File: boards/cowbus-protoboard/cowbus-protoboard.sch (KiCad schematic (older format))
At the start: 9 parts

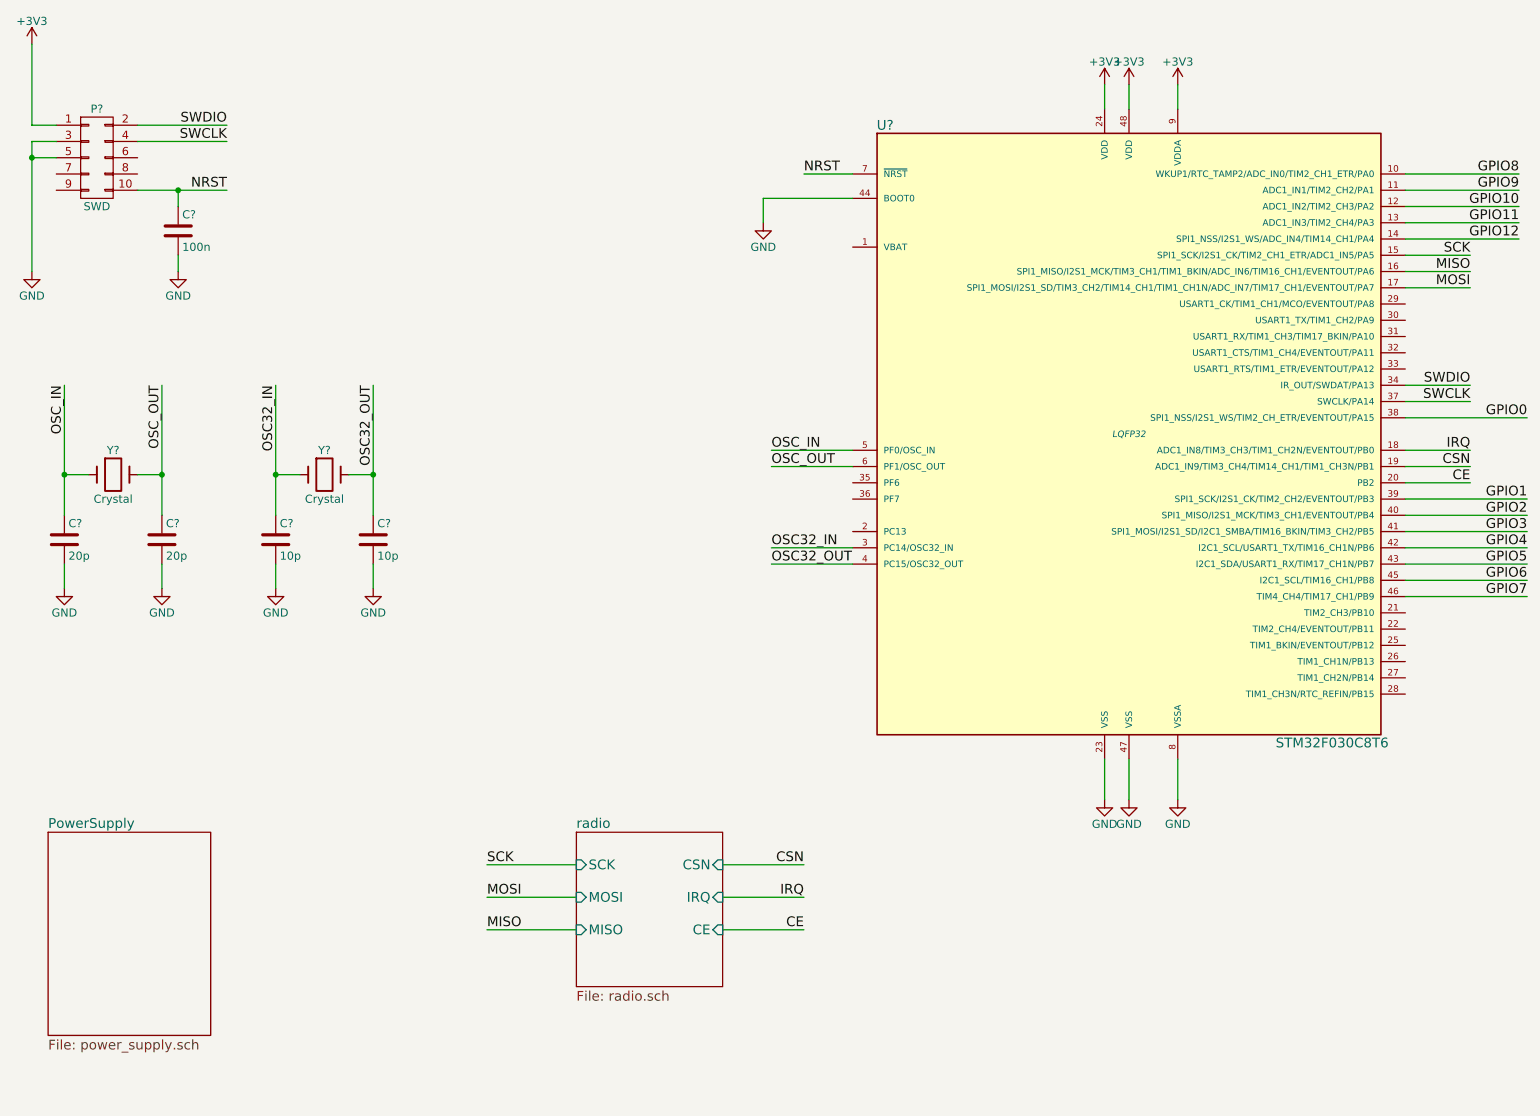
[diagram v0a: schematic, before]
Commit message: mad emcu second hierarchy, added top level, added empty periph
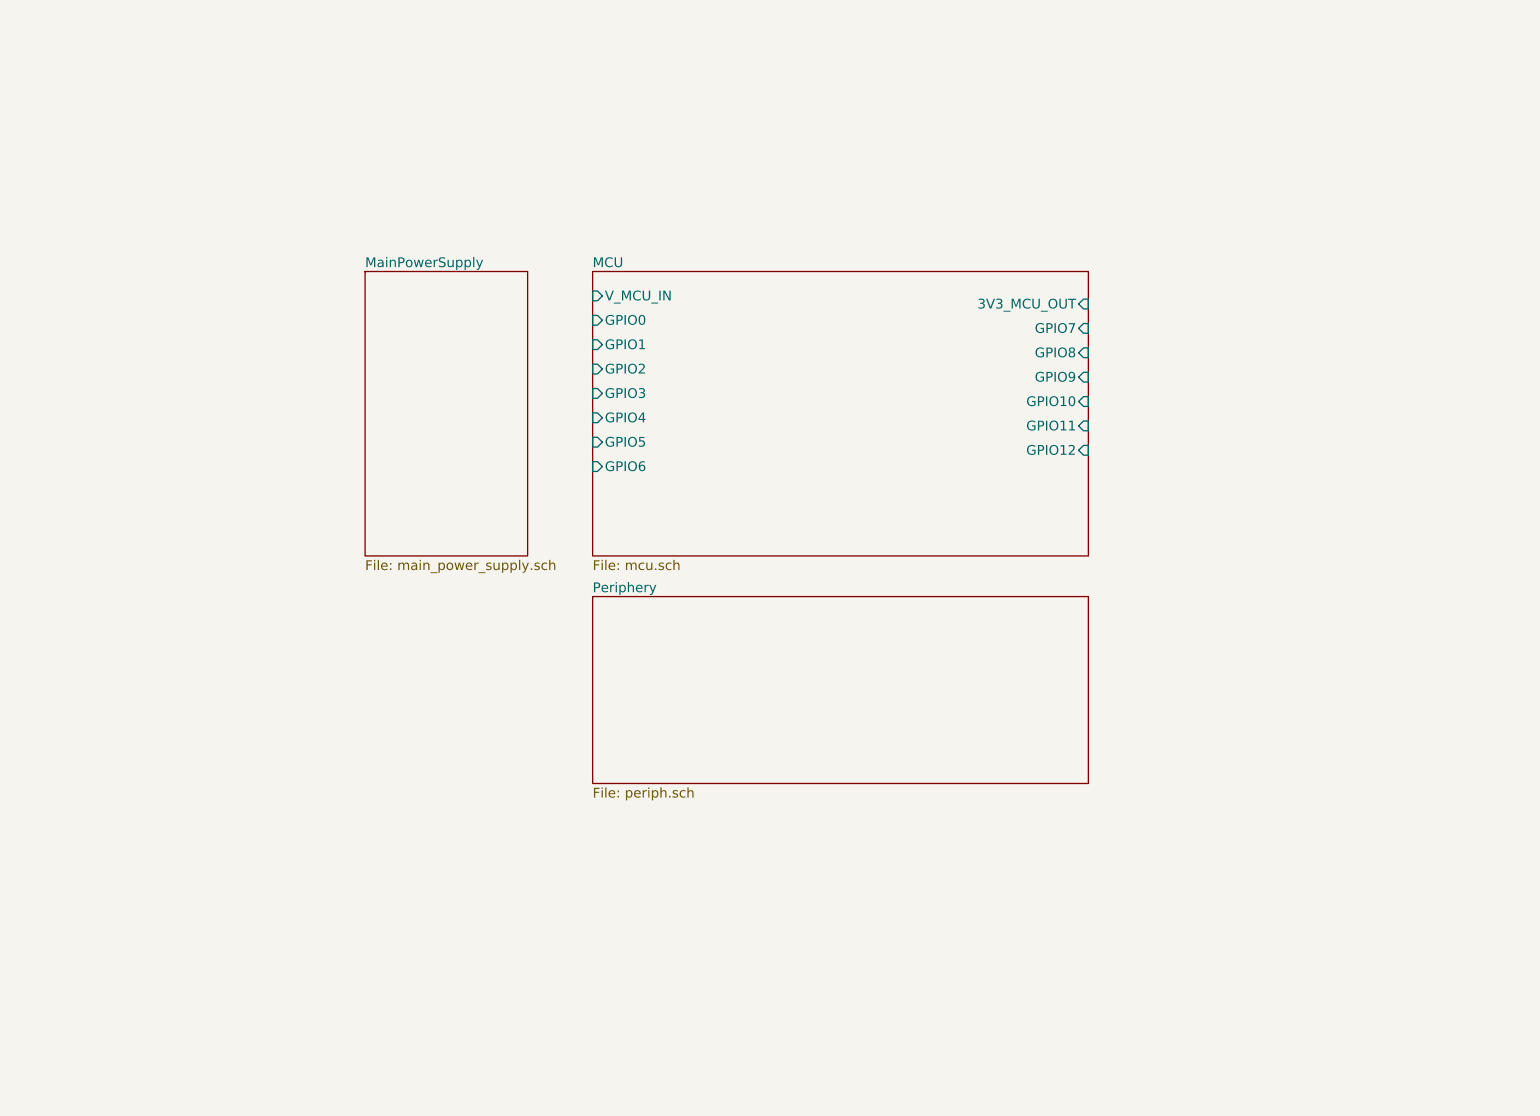
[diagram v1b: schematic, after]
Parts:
- removed C? (x2): 20p, symbol C
- removed C? (x2): 10p, symbol C
- removed C?: 100n, symbol C
- removed P?: SWD, symbol CONN_02X05
- removed U?: STM32F030C8T6, LQFP32, symbol STM32F030C8T6
- removed Y? (x2): Crystal, symbol Crystal

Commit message: Buzzer added, RGB added, further GPIO added
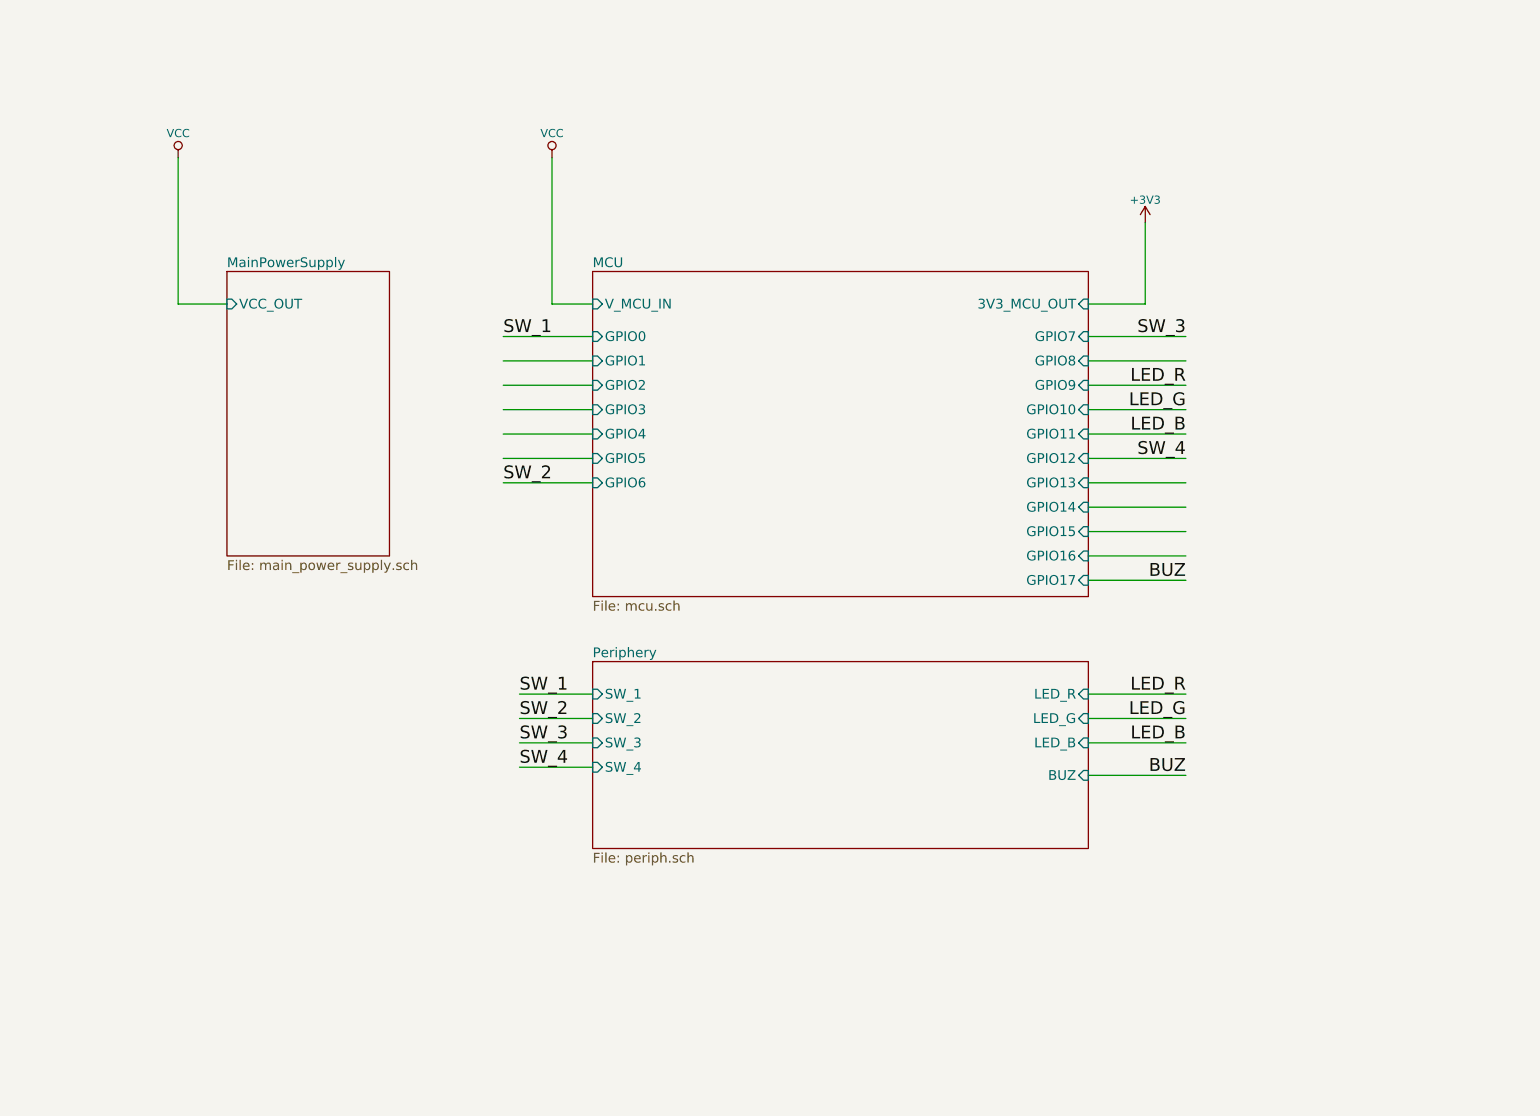
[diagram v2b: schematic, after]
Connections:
- net labels added: +3V3, BUZ, LED_B, LED_G, LED_R, SW_1, SW_2, SW_3, SW_4, VCC
- wire segments 0 -> 32
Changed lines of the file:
@@
 $EndDescr
 $Sheet
-S 4450 2300 3050 1750
+S 4450 2300 3050 2000
 U 55A613A8
 F0 "MCU" 60
 F1 "mcu.sch" 60
-F2 "V_MCU_IN" I L 4450 2450 60
+F2 "V_MCU_IN" I L 4450 2500 60
 F3 "3V3_MCU_OUT" I R 7500 2500 60
-F4 "GPIO1" I L 4450 2750 60
-F5 "GPIO2" I L 4450 2900 60
-F6 "GPIO3" I L 4450 3050 60
-F7 "GPIO4" I L 4450 3200 60
-F8 "GPIO5" I L 4450 3350 60
-F9 "GPIO6" I L 4450 3500 60
-F10 "GPIO7" I R 7500 2650 60
-F11 "GPIO0" I L 4450 2600 60
-F12 "GPIO8" I R 7500 2800 60
-F13 "GPIO9" I R 7500 2950 60
-F14 "GPIO10" I R 7500 3100 60
-F15 "GPIO11" I R 7500 3250 60
-F16 "GPIO12" I R 7500 3400 60
+F4 "GPIO1" I L 4450 2850 60
+F5 "GPIO2" I L 4450 3000 60
+F6 "GPIO3" I L 4450 3150 60
+F7 "GPIO4" I L 4450 3300 60
+F8 "GPIO5" I L 4450 3450 60
+F9 "GPIO6" I L 4450 3600 60
+F10 "GPIO7" I R 7500 2700 60
+F11 "GPIO0" I L 4450 2700 60
+F12 "GPIO8" I R 7500 2850 60
+F13 "GPIO9" I R 7500 3000 60
+F14 "GPIO10" I R 7500 3150 60
+F15 "GPIO11" I R 7500 3300 60
+F16 "GPIO12" I R 7500 3450 60
+F17 "GPIO13" I R 7500 3600 60
+F18 "GPIO14" I R 7500 3750 60
+F19 "GPIO15" I R 7500 3900 60
+F20 "GPIO16" I R 7500 4050 60
+F21 "GPIO17" I R 7500 4200 60
 $EndSheet
 $Sheet
-S 3050 2300 1000 1750
+S 2200 2300 1000 1750
 U 55A63C73
 F0 "MainPowerSupply" 60
 F1 "main_power_supply.sch" 60
+F2 "VCC_OUT" I L 2200 2500 60
 $EndSheet
 $Sheet
-S 4450 4300 3050 1150
+S 4450 4700 3050 1150
 U 55A6421F
 F0 "Periphery" 60
 F1 "periph.sch" 60
+F2 "SW_1" I L 4450 4900 60
+F3 "SW_2" I L 4450 5050 60
+F4 "SW_3" I L 4450 5200 60
+F5 "SW_4" I L 4450 5350 60
+F6 "LED_R" I R 7500 4900 60
+F7 "LED_G" I R 7500 5050 60
+F8 "LED_B" I R 7500 5200 60
+F9 "BUZ" I R 7500 5400 60
 $EndSheet
+Wire Wire Line
+	7500 4900 8100 4900
+Wire Wire Line
+	7500 5050 8100 5050
+Wire Wire Line
+	7500 5200 8100 5200
+Text Label 8100 4900 2    79   ~ 0
+LED_R
+Text Label 8100 5050 2    79   ~ 0
+LED_G
+Text Label 8100 5200 2    79   ~ 0
+LED_B
+Wire Wire Line
+	7500 3000 8100 3000
+Wire Wire Line
+	7500 3150 8100 3150
+Wire Wire Line
+	7500 3300 8100 3300
+Text Label 8100 3000 2    79   ~ 0
+LED_R
+Text Label 8100 3150 2    79   ~ 0
+LED_G
+Text Label 8100 3300 2    79   ~ 0
+LED_B
+$Comp
+L VCC #PWR?
+U 1 1 55A6ED40
+P 1900 1600
+F 0 "#PWR?" H 1900 1450 50  0001 C CNN
+F 1 "VCC" H 1900 1750 50  0000 C CNN
+F 2 "" H 1900 1600 60  0000 C CNN
+F 3 "" H 1900 1600 60  0000 C CNN
+	1    1900 1600
+	1    0    0    -1
+$EndComp
+$Comp
+L VCC #PWR?
+U 1 1 55A73D74
+P 4200 1600
+F 0 "#PWR?" H 4200 1450 50  0001 C CNN
+F 1 "VCC" H 4200 1750 50  0000 C CNN
+F 2 "" H 4200 1600 60  0000 C CNN
+F 3 "" H 4200 1600 60  0000 C CNN
+	1    4200 1600
+	1    0    0    -1
+$EndComp
+$Comp
+L +3V3 #PWR?
+U 1 1 55A75A13
+P 7850 2000
+F 0 "#PWR?" H 7850 1850 50  0001 C CNN
+F 1 "+3V3" H 7850 2140 50  0000 C CNN
+F 2 "" H 7850 2000 60  0000 C CNN
+F 3 "" H 7850 2000 60  0000 C CNN
+	1    7850 2000
+	1    0    0    -1
+$EndComp
+Wire Wire Line
+	7500 2500 7850 2500
+Wire Wire Line
+	7850 2500 7850 2000
+Wire Wire Line
+	2200 2500 1900 2500
+Wire Wire Line
+	1900 2500 1900 1600
+Wire Wire Line
+	4450 2500 4200 2500
+Wire Wire Line
+	4200 2500 4200 1600
+Wire Wire Line
+	7500 3450 8100 3450
+Text Label 8100 3450 2    79   ~ 0
+SW_4
+Wire Wire Line
+	4450 4900 4000 4900
+Wire Wire Line
+	4450 5050 4000 5050
+Wire Wire Line
+	4450 5200 4000 5200
+Wire Wire Line
+	4450 5350 4000 5350
+Text Label 4000 5350 0    79   ~ 0
+SW_4
+Wire Wire Line
+	4450 2700 3900 2700
+Wire Wire Line
+	4450 2850 3900 2850
+Wire Wire Line
+	4450 3000 3900 3000
+Wire Wire Line
+	4450 3150 3900 3150
+Wire Wire Line
+	4450 3300 3900 3300
+Wire Wire Line
+	4450 3450 3900 3450
+Wire Wire Line
+	4450 3600 3900 3600
+Wire Wire Line
+	7500 2700 8100 2700
+Wire Wire Line
+	7500 2850 8100 2850
+Text Label 8100 2700 2    79   ~ 0
+SW_3
+Text Label 4000 5200 0    79   ~ 0
+SW_3
+Text Label 4000 5050 0    79   ~ 0
+SW_2
+Text Label 4000 4900 0    79   ~ 0
+SW_1
+Text Label 3900 3600 0    79   ~ 0
+SW_2
+Text Label 3900 2700 0    79   ~ 0
+SW_1
+Wire Wire Line
+	7500 3600 8100 3600
+Wire Wire Line
+	7500 3750 8100 3750
+Wire Wire Line
+	7500 3900 8100 3900
+Wire Wire Line
+	7500 4050 8100 4050
+Wire Wire Line
+	7500 4200 8100 4200
+Wire Wire Line
+	7500 5400 8100 5400
+Text Label 8100 5400 2    79   ~ 0
+BUZ
+Text Label 8100 4200 2    79   ~ 0
+BUZ
 $EndSCHEMATC

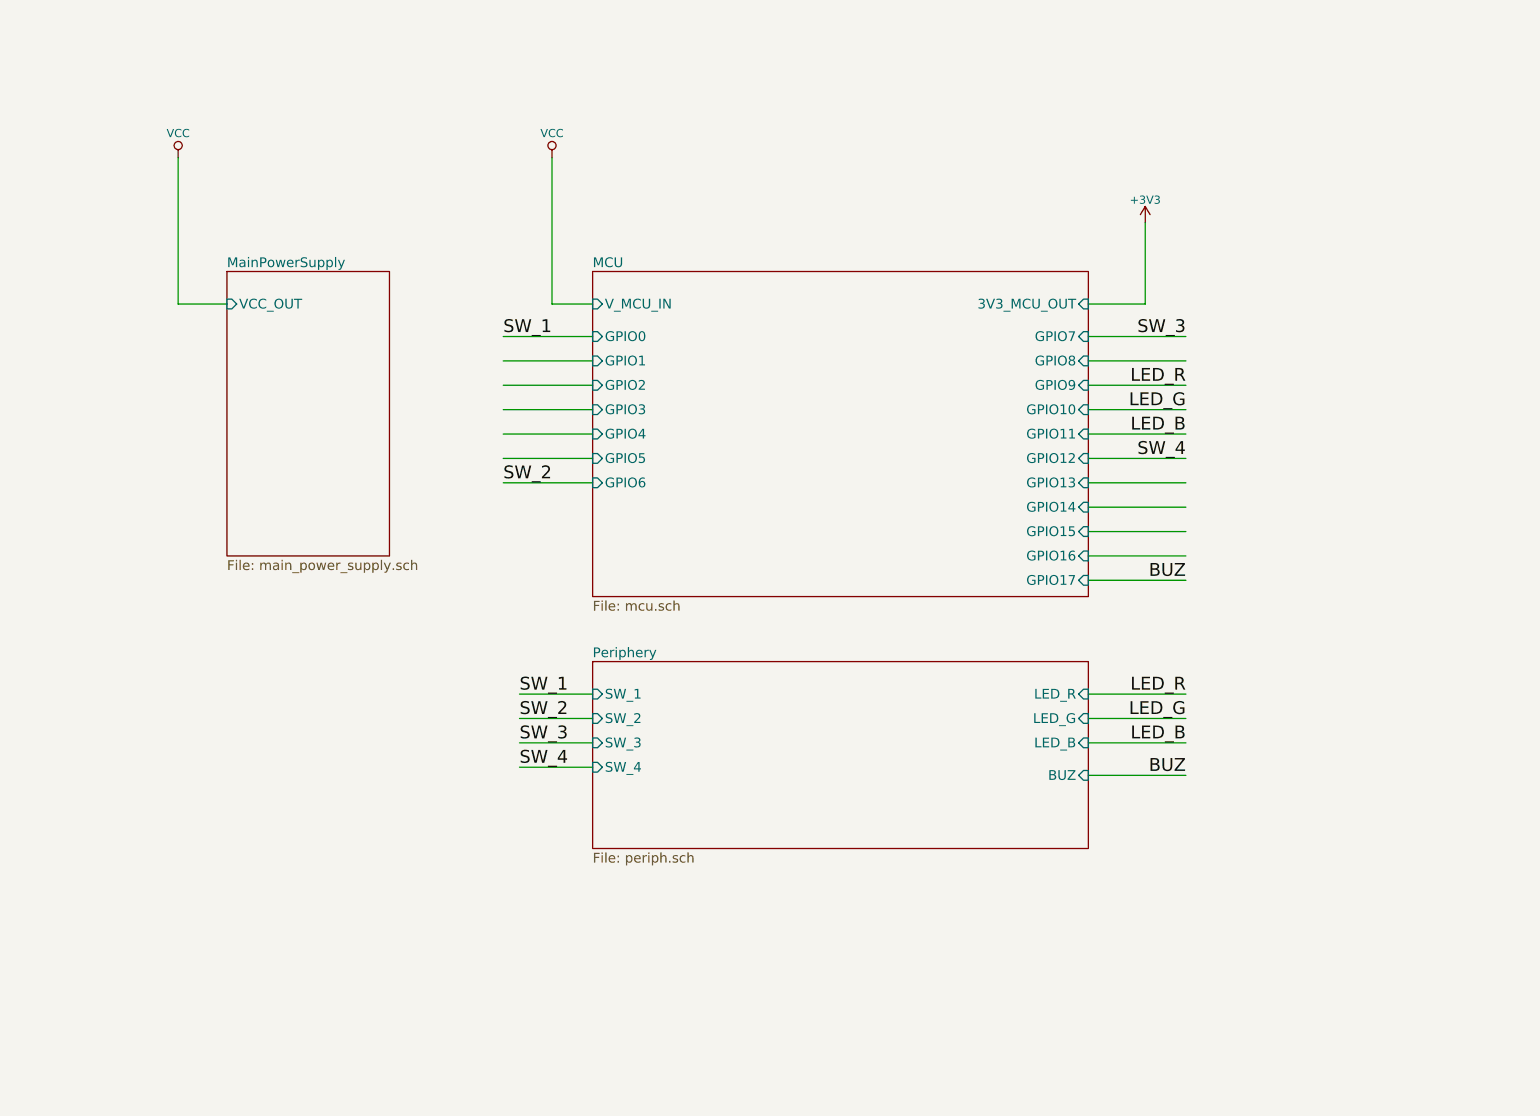
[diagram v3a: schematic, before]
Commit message: added temp sensor, added usart for printf-debugging
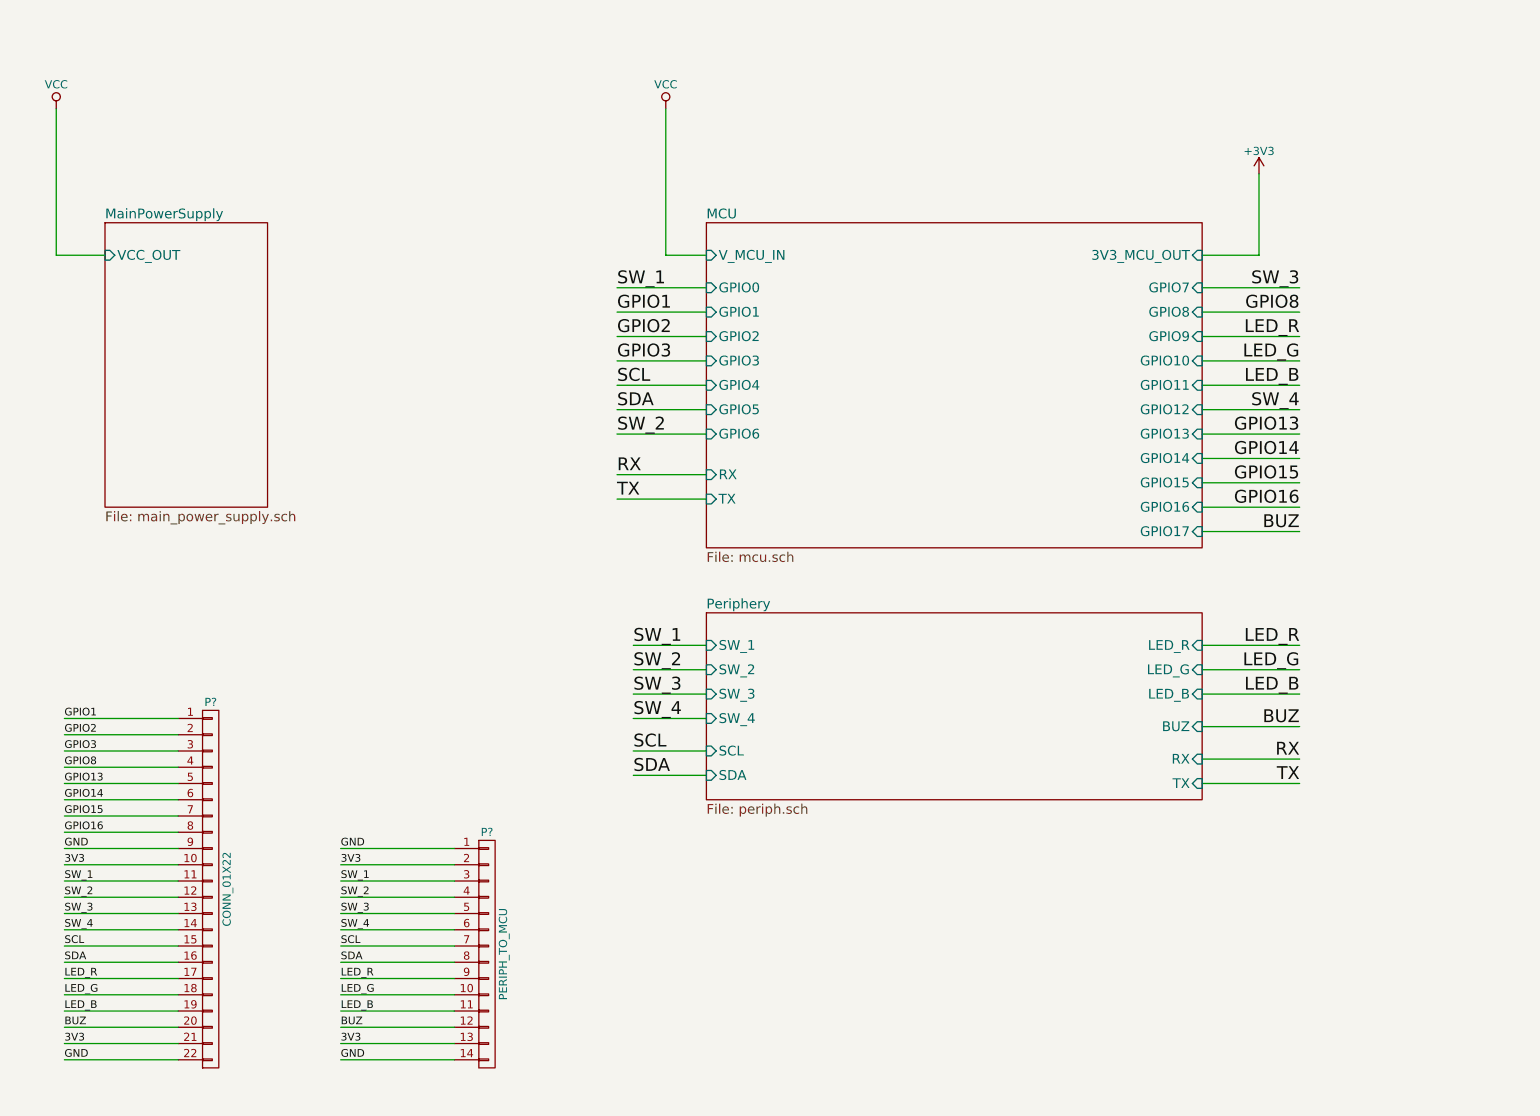
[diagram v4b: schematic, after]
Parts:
- added P?: PERIPH_TO_MCU, symbol CONN_01X14
- added P?: CONN_01X22, symbol CONN_01X22
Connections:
- net labels added: 3V3, GND, GPIO1, GPIO13, GPIO14, GPIO15, GPIO16, GPIO2, GPIO3, GPIO8, RX, SCL, SDA, TX
- wire segments 32 -> 74
